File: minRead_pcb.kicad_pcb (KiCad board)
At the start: 2 copper layers, 62.4 x 117.6 mm, 119 parts, among them J1 USB_C_Receptacle, J2 FH34SRJ-24S-0.5SH_50_, J3 FH34SRJ-6S-0.5SH_50_, J5 Conn_01x02, J7 Micro_SD_Card, Q10 BSS138, Q11 BSS138, Q16 MMBT3906, Q17 MMBT3904, Q18 AO3419, Q4 [BSS138] AO3400A, Q5 AO3419, Q6 AO3419, SW1 SW_Push, SW10 SW_Push, SW11 SW_Push, SW2 SW_Push, SW3 SW_Push, SW4 SW_Push, SW6 SW_Push, SW8 SW_Push, SW9 SW_Push, U1 TPD4E1U06DBVR, U11 AP3031KTR, U3 AP2112K-3.3, U4 ESP32-S3-WROOM-1, U6 TPD4E1U06DBVR, U7 MCP73832-2-OT

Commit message: reset
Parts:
- D2: footprint LED_THT:LED_D3.0mm -> LED_SMD:LED_0805_2012Metric_Pad1.15x1.40mm_HandSolder
- SW11: footprint mjtp1117:MJTP1117 -> TestPoint:TestPoint_Bridge_Pitch2.54mm_Drill1.0mm
- SW6: footprint Button_Switch_THT:SW_PUSH_1P1T_6x3.5mm_H4.3_APEM_MJTP1243 -> TestPoint:TestPoint_Bridge_Pitch2.54mm_Drill1.0mm
- moved R2 143.2 mm to (104.4, 36.7), turned to 90 degrees
- moved R3 140.6 mm to (104.3, 40.5)
- moved U1 107.8 mm to (84.2, 120.5), turned to 180 degrees
- moved R9 104.0 mm to (93.2, 136.8), turned to 0 degrees
- moved C37 96.5 mm to (86.2, 130.3), turned to 90 degrees
- moved C36 91.3 mm to (85.2, 124.5), turned to 90 degrees
- moved D2 80.1 mm to (79.5, 67.8)
- moved SW10 57.6 mm to (78.3, 38.7)
- moved R53 42.6 mm to (88.0, 140.2), turned to 0 degrees
- moved R54 38.4 mm to (88.0, 137.9), turned to 0 degrees
- moved R55 35.5 mm to (88.0, 135.9), turned to 0 degrees
- moved R8 30.4 mm to (93.2, 138.8), turned to 0 degrees
- moved SW6 13.3 mm to (-35.8, 71.0)
- moved J7 6.32 mm to (96.0, 126.3)
- moved R4 4.32 mm to (122.8, 120.2)
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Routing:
- net 3V3: track 59.6 -> 257.4 mm, vias 2 -> 9
- net SD_DAT3: track 0.00 -> 166.7 mm, vias 0 -> 2
- net SD_DAT1: track 0.00 -> 161.1 mm, vias 0 -> 2
- net SD_DAT2: track 0.00 -> 156.0 mm, vias 0 -> 3
- net SD_DAT0: track 0.00 -> 149.1 mm, vias 0 -> 2
- net SD_CLK: track 0.00 -> 132.4 mm, vias 0 -> 2
- net SD_CMD: track 0.00 -> 130.1 mm, vias 0 -> 2
- net EPD_RST: track 9.36 -> 125.1 mm
- net EPD_MOSI: track 34.4 -> 123.4 mm, vias 2 -> 4
- net EPD_SCK: track 32.9 -> 121.6 mm
- net EPD_CS: track 31.6 -> 120.2 mm, vias 2 -> 0
- net EPD_DC: track 30.4 -> 118.0 mm, vias 2 -> 0
- net EPD_BUSY: track 28.5 -> 115.4 mm, vias 2 -> 0
- net LED_ACTIVATE: track 2.22 -> 52.2 mm, vias 0 -> 5
- net USB_VBUS: track 9.89 -> 32.1 mm
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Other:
- board size 62.4 x 117.6 mm -> 62.4 x 115 mm
- board text removed: "LED"

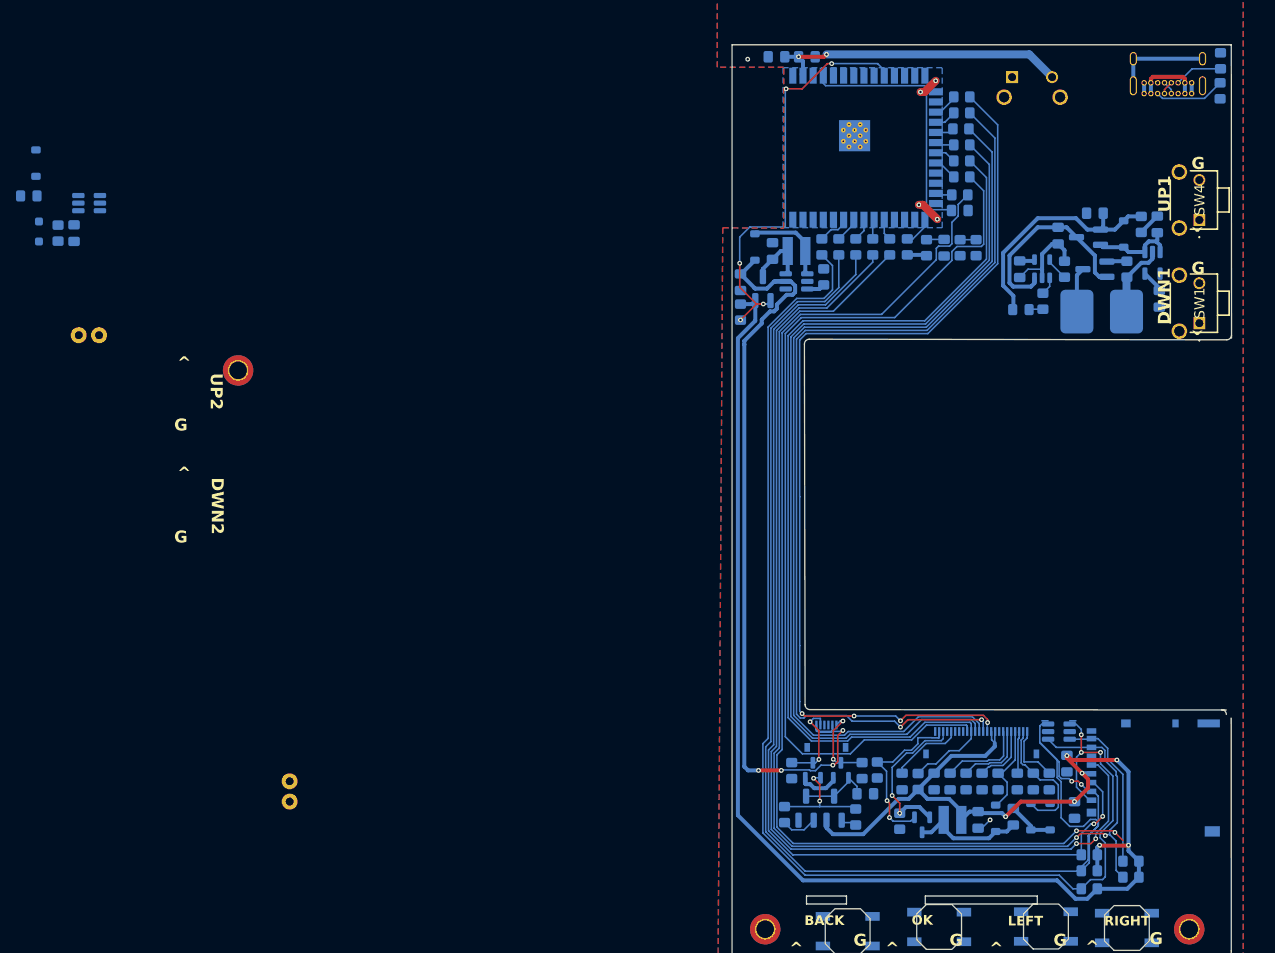
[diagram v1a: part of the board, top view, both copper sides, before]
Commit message: mostly routed
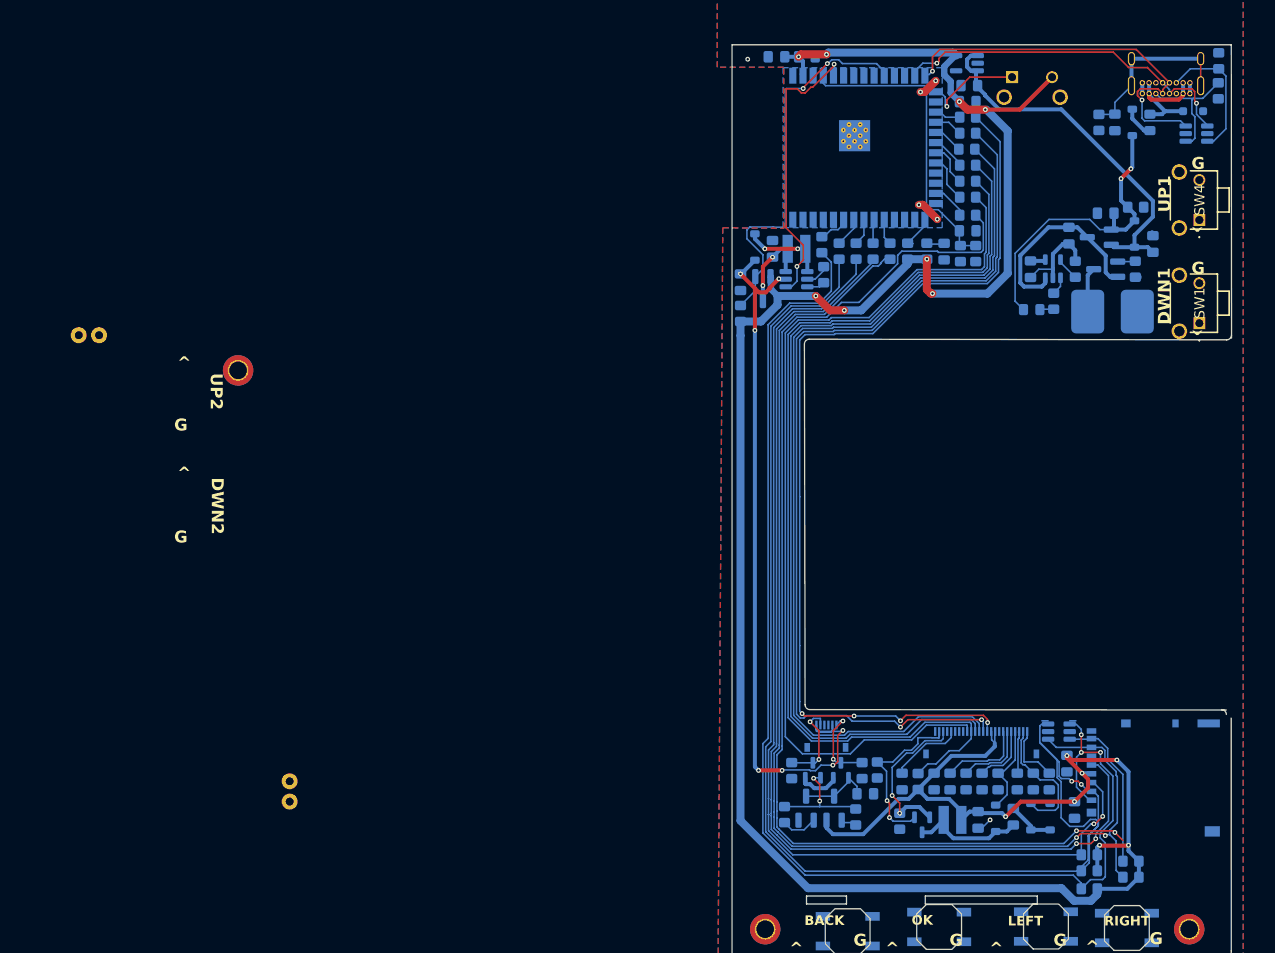
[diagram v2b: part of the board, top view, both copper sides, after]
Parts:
- added C12: 1u, Capacitor_SMD:C_0805_2012Metric_Pad1.18x1.45mm_HandSolder, B.Cu at (73.0, 39.8)
- C6: value 22u -> 1u
- moved CR1 145.0 mm to (101.0, 43.0), turned to 0 degrees
- moved F1 140.4 mm to (95.6, 44.4), turned to -90 degrees
- moved U6 138.7 mm to (101.4, 45.8), turned to 180 degrees
- moved D1 137.1 mm to (93.4, 44.4), turned to 90 degrees
- moved C1 130.8 mm to (91.2, 44.4)
- moved R1 130.8 mm to (89.2, 44.4)
- moved C6 34.4 mm to (72.8, 41.8), turned to 0 degrees
- moved U3 34.1 mm to (72.7, 37.0), turned to 180 degrees
- moved C8 2.72 mm to (72.8, 58.0)
- moved R26 2.72 mm to (72.8, 56.0)
- moved R30 2.64 mm to (72.8, 45.8)
- moved R31 2.64 mm to (72.7, 47.7)
- moved R33 2.64 mm to (72.8, 51.8)
- moved R29 2.64 mm to (72.8, 43.7)
- moved R32 2.64 mm to (72.8, 49.8)
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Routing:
- net 3V3: track 257.4 -> 326.3 mm, vias 9 -> 15
- net DP: track 1.70 -> 49.4 mm, vias 0 -> 2
- net DN: track 1.70 -> 44.5 mm, vias 0 -> 2
- net PWM_LED: track 0.00 -> 36.3 mm, vias 0 -> 2
- net LDO_IN: track 11.1 -> 46.4 mm
- net PWR_BUTTON: track 0.00 -> 12.8 mm, vias 0 -> 1
- net CC2: track 6.02 -> 16.9 mm
- net Net-(J1-SHIELD): track 12.0 -> 21.8 mm
- net B-: track 33.8 -> 24.7 mm
- net USB_VBUS: track 32.1 -> 41.2 mm, vias 0 -> 2
- net LED_SW: track 100.0 -> 92.6 mm, vias 4 -> 7
- net /VBUS_PRE: track 8.15 -> 15.3 mm
- net CC1: track 8.86 -> 15.4 mm
- net Net-(D1-A): track 0.00 -> 4.00 mm
- net BAT_MONIT: track 34.6 -> 38.4 mm
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
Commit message: switch buttons to mid mount
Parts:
- SW1, SW4: footprint mjtp1117:MJTP1117 -> DEAN:SKSNLAE010; moved to B.Cu
- SW10: footprint mjtp1117:MJTP1117 -> DEAN:SKSNLAE010
- moved SW1 3.77 mm to (103.9, 66.4), turned to -90 degrees
- moved SW4 2.18 mm to (103.9, 56.4), turned to -90 degrees
- moved SW9 0.59 mm to (57.9, 144.9)
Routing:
- net SD_DAT1: track 162.5 -> 167.3 mm
- net SD_DAT0: track 149.0 -> 153.3 mm
- net SD_CLK: track 132.0 -> 136.2 mm
- net SD_CMD: track 129.7 -> 133.5 mm
- net SD_DAT2: track 156.7 -> 158.4 mm
- net 3V3: track 326.3 -> 328.0 mm
- net SD_DAT3: track 166.4 -> 165.5 mm
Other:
- outline, holes or cut-outs redrawn

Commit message: pre drs
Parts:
- removed C1: 1n, Capacitor_SMD:C_0805_2012Metric_Pad1.18x1.45mm_HandSolder
- removed C29: 2.2n, Capacitor_SMD:C_0805_2012Metric_Pad1.18x1.45mm_HandSolder
- removed H1, H2, H3, H4: MountingHole_Pad, MountingHole:MountingHole_2.2mm_M2_DIN965_Pad_TopBottom
- removed R1: 1M, Resistor_SMD:R_0805_2012Metric_Pad1.20x1.40mm_HandSolder
- moved C28 152.5 mm to (62.5, 63.6)
- moved R28 139.4 mm to (79.5, 57.6), turned to 90 degrees
- moved R11 125.2 mm to (99.2, 54.9), turned to 90 degrees
- moved R61 119.4 mm to (99.2, 68.8), turned to 90 degrees
- moved R60 113.1 mm to (89.5, 144.1), turned to -90 degrees
- moved SW6 107.0 mm to (71.2, 69.8)
- moved SW11 104.8 mm to (74.3, 69.8), turned to 0 degrees
- moved C27 101.6 mm to (60.3, 65.7)
- moved R18 81.3 mm to (77.3, 144.1), turned to -90 degrees
- moved R4 79.3 mm to (47.2, 144.1), turned to 90 degrees
- moved R19 77.9 mm to (61.2, 144.1), turned to -90 degrees
- moved R20 77.1 mm to (49.2, 144.1), turned to -90 degrees
- moved C5 27.1 mm to (58.0, 36.2), turned to 0 degrees
- moved R7 25.0 mm to (61.8, 36.2), turned to 180 degrees
- moved SW10 6.27 mm to (84.6, 38.3)
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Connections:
- J1 pad S1: Net-(J1-SHIELD) -> B-
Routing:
- net BUTTON_ADC_1: track 0.00 -> 167.1 mm, vias 0 -> 4
- net COLOR_SEL: track 13.6 -> 125.4 mm, vias 2 -> 6
- net BUTTON_ADC_2: track 0.00 -> 81.1 mm, vias 0 -> 2
- net Net-(Q10-S): track 7.50 -> 83.2 mm, vias 0 -> 2
- net DP: track 49.4 -> 15.9 mm
- net DN: track 44.5 -> 13.9 mm
- net 3V3: track 328.0 -> 304.6 mm, vias 15 -> 16
- net Net-(J1-SHIELD): track 21.8 -> 0.00 mm
- net B-: track 24.7 -> 39.4 mm, vias 6 -> 17
- net USB_VBUS: track 41.2 -> 51.8 mm, vias 2 -> 4
- net ESP32_EN: track 2.22 -> 9.97 mm
- net LED_SW: track 92.6 -> 99.7 mm
- net PWR_BUTTON: track 12.8 -> 19.8 mm, vias 1 -> 4
- net P+: track 25.0 -> 31.8 mm, vias 0 -> 2
- net W-: track 10.1 -> 13.1 mm
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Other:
- board size 62.4 x 115 mm -> 62.4 x 115.1 mm
- board text added: "apparently having empty space instead of fr4 is beneficial"
- board text added: "buttons are 1.4mm apart measured from center. assume each button has the part where ur thumb presses that part that ur thumb presses will be 1cm in length therefore cutout must extend 0.5cm past center of each button just take a look at iphone volume buttons"
- board text removed: "DWN1"
- board text removed: "EPaper Connector"
- board text removed: "UP1"

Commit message: fix some drc
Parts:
- removed G*** (x2): LOGO, LOGO
- moved SW11 30.4 mm to (77.2, 39.6), turned to 90 degrees
- moved C28 5.71 mm to (67.3, 60.5), turned to -90 degrees
- moved C27 1.12 mm to (60.8, 64.7)
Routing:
- net DN: track 13.9 -> 45.9 mm
- net DP: track 15.9 -> 46.4 mm
- net 3V3: track 304.6 -> 327.6 mm, vias 16 -> 18
- net ESP32_EN: track 9.97 -> 28.1 mm, vias 0 -> 2
- net ESP32_IO0: track 5.43 -> 22.2 mm, vias 0 -> 4
- net B-: track 39.4 -> 49.6 mm, vias 17 -> 65
- net BUTTON_ADC_2: track 81.1 -> 77.2 mm
- net SD_DAT3: track 167.2 -> 164.2 mm
- net COLOR_SEL: track 125.4 -> 126.7 mm
- net BUTTON_ADC_1: track 167.1 -> 166.0 mm
- net LED_ACTIVATE: track 47.7 -> 48.5 mm
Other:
- board text removed: "24"
- board text removed: "3v3"
- board text removed: "DWN2"
- board text removed: "ESP32-S3 WROOM"
- board text removed: "G"
- board text removed: "PWR"
- board text removed: "Thank you! - Ian C"
- board text removed: "UP2"
- board text removed: "^"
- board text removed: "cat by @tomisit0"
- board text removed: "microSD if you please"

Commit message: fin
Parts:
- moved L3 0.75 mm to (50.3, 60.5)
- moved U11 0.65 mm to (51.4, 64.3)
- moved R59 0.10 mm to (84.7, 66.3)
- moved Q18 0.08 mm to (47.2, 65.2)
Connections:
- J7 pad SH: (no net) -> B-
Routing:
- net B-: track 49.6 -> 76.5 mm, vias 65 -> 66
- net BUTTON_ADC_1: track 166.0 -> 167.0 mm
- net Net-(Q10-S): track 83.2 -> 84.1 mm
- net SD_DAT2: track 160.0 -> 160.8 mm
- net DN: track 45.9 -> 46.5 mm
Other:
- board size 62.4 x 115.1 mm -> 62.4 x 115 mm

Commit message: drc
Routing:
- net B-: track 76.5 -> 92.4 mm, vias 66 -> 68
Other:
- board text added: "from dean"
- board text added: "to my fav bean..."
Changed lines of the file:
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@@
 		(sheetname "/")
 		(sheetfile "minRead_pcb.kicad_sch")
-		(units
-			(unit
-				(name "A")
-				(pins "1" "2")
-			)
-		)
 		(attr smd)
 		(duplicate_pad_numbers_are_jumpers no)
@@
 		)
 		(fp_circle
-			(center -4.894 1.85)
-			(end -4.6908 1.85)
+			(center -3.6 1.05)
+			(end -3.3968 1.05)
 			(stroke
 				(width 0.1524)
@@
 		)
 		(fp_circle
-			(center -3.1033 3.2851)
-			(end -2.9001 3.2851)
+			(center -3.6 1.05)
+			(end -3.3968 1.05)
 			(stroke
 				(width 0.1524)
@@
 		(sheetname "/")
 		(sheetfile "minRead_pcb.kicad_sch")
-		(units
-			(unit
-				(name "A")
-				(pins "1" "2")
-			)
-		)
 		(attr smd)
 		(duplicate_pad_numbers_are_jumpers no)
@@
 		)
 		(fp_circle
-			(center -4.894 1.85)
-			(end -4.6908 1.85)
+			(center -3.6 1.05)
+			(end -3.3968 1.05)
 			(stroke
 				(width 0.1524)
@@
 		)
 		(fp_circle
-			(center -3.1033 3.2851)
-			(end -2.9001 3.2851)
+			(center -3.6 1.05)
+			(end -3.3968 1.05)
 			(stroke
 				(width 0.1524)
@@
 		(tags "resistor handsolder")
 		(property "Reference" "R8"
-			(at 2.445375 0 0)
+			(at 1.15 1.4 0)
 			(layer "B.SilkS")
 			(effects
@@
 		(sheetname "/")
 		(sheetfile "minRead_pcb.kicad_sch")
-		(units
-			(unit
-				(name "A")
-				(pins "1" "2")
-			)
-		)
 		(attr smd)
 		(duplicate_pad_numbers_are_jumpers no)
@@
 		)
 		(fp_circle
-			(center -4.894 1.85)
-			(end -4.6908 1.85)
+			(center -3.6 1.05)
+			(end -3.3968 1.05)
 			(stroke
 				(width 0.1524)
@@
 		)
 		(fp_circle
-			(center -3.1033 3.2851)
-			(end -2.9001 3.2851)
+			(center -3.6 1.05)
+			(end -3.3968 1.05)
 			(stroke
 				(width 0.1524)
@@
 		(sheetname "/")
 		(sheetfile "minRead_pcb.kicad_sch")
-		(units
-			(unit
-				(name "A")
-				(pins "1" "2")
-			)
-		)
 		(attr smd)
 		(duplicate_pad_numbers_are_jumpers no)
@@
 		)
 		(fp_circle
-			(center -4.894 1.85)
-			(end -4.6908 1.85)
+			(center -3.6 1.05)
+			(end -3.3968 1.05)
 			(stroke
 				(width 0.1524)
@@
 		)
 		(fp_circle
-			(center -3.1033 3.2851)
-			(end -2.9001 3.2851)
+			(center -3.6 1.05)
+			(end -3.3968 1.05)
 			(stroke
 				(width 0.1524)
@@
 	(gr_poly
 		(pts
+			(arc
+				(start 104.6 140.65)
+				(mid 104.476597 140.116603)
+				(end 103.935222 140.198177)
+			)
+			(arc
+				(start 103.935222 140.198177)
+				(mid 103.393847 140.116603)
+				(end 103.270444 140.65)
+			)
+			(xy 103.95 141.45)
+		)
+		(stroke
+			(width 0)
+			(type solid)
+		)
+		(fill yes)
+		(layer "B.SilkS")
+	)
+	(gr_poly
+		(pts
 			(xy 43.35 34.7) (xy 43.35 140.1) (xy 105.75 140.1) (xy 105.75 34.7)
 		)
@@
 		)
 	)
+	(gr_text "   from \ndean\n"
+		(at 104.9 143.45 0)
+		(layer "B.SilkS")
+		(effects
+			(font
+				(size 1.2 1.2)
+			)
+			(justify left bottom mirror)
+		)
+	)
+	(gr_text "to my fav\nbean..."
+		(at 104.95 138.15 0)
+		(layer "B.SilkS")
+		(effects
+			(font
+				(size 1.2 1.2)
+			)
+			(justify left bottom mirror)
+		)
+	)
 	(gr_text "LP284550/LP304550"
 		(at 71.6 94.6 0)
@@
 	)
 	(via
+		(at 91.85 69.5)
+		(size 0.6)
+		(drill 0.3)
+		(layers "F.Cu" "B.Cu")
+		(net "B-")
+	)
+	(via
 		(at 60.7 133.7)
 		(size 0.6)
@@
 	)
 	(via
+		(at 65.65 129.8)
+		(size 0.6)
+		(drill 0.3)
+		(layers "F.Cu" "B.Cu")
+		(net "B-")
+	)
+	(via
 		(at 97 122.4)
 		(size 0.6)
@@
 	)
 	(via
-		(at 81 130.875)
+		(at 80.05 129.7)
 		(size 0.6)
 		(drill 0.3)
@@
 	)
 	(via
-		(at 96.8 62.3)
+		(at 97.7 49.2)
 		(size 0.6)
 		(drill 0.3)
@@
 	)
 	(via
-		(at 97.7 49.2)
+		(at 97.2 62.85)
 		(size 0.6)
 		(drill 0.3)
 		(layers "F.Cu" "B.Cu")
-		(free yes)
 		(net "B-")
 	)
@@
 	)
 	(via
-		(at 101.9 139.2)
+		(at 97.2 138.55)
 		(size 0.6)
 		(drill 0.3)
@@
 	)
 	(segment
+		(start 64.6 130.85)
+		(end 65.65 129.8)
+		(width 0.2)
+		(layer "B.Cu")
+		(net "B-")
+	)
+	(segment
 		(start 50.939999 38.56157)
 		(end 50.939999 39.360001)
@@
 	)
 	(segment
+		(start 95 67.6)
+		(end 93.75 67.6)
+		(width 1)
+		(layer "B.Cu")
+		(net "B-")
+	)
+	(segment
+		(start 95 67.6)
+		(end 97.2 65.4)
+		(width 1)
+		(layer "B.Cu")
+		(net "B-")
+	)
+	(segment
 		(start 88.275 130.675)
 		(end 86.8625 130.675)
@@
 	)
 	(segment
+		(start 95 67.6)
+		(end 94.6 67.6)
+		(width 1)
+		(layer "B.Cu")
+		(net "B-")
+	)
+	(segment
 		(start 95.8 54.55)
 		(end 95.8 54)
@@
 	)
 	(segment
+		(start 97.2 65.4)
+		(end 97.2 62.85)
+		(width 1)
+		(layer "B.Cu")
+		(net "B-")
+	)
+	(segment
 		(start 96.850002 57.7)
 		(end 96.850002 57.6625)
@@
 	)
 	(segment
+		(start 64.6 130.875)
+		(end 64.6 130.85)
+		(width 0.2)
+		(layer "B.Cu")
+		(net "B-")
+	)
+	(segment
+		(start 93.75 67.6)
+		(end 91.85 69.5)
+		(width 1)
+		(layer "B.Cu")
+		(net "B-")
+	)
+	(segment
 		(start 84.450002 60.393394)
 		(end 85.705896 59.1375)
@@
 		(width 1)
 		(layer "B.Cu")
+		(net "B-")
+	)
+	(segment
+		(start 94.6 67.6)
+		(end 91.5 64.5)
+		(width 1)
+		(layer "B.Cu")

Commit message: switch to 5k1 prog
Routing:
- net B-: track 92.4 -> 107.3 mm
- net LDO_IN: track 49.3 -> 51.1 mm
- net LED_SW: track 99.9 -> 98.9 mm
